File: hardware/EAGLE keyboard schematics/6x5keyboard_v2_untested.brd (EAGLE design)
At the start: 117.8 x 116.8 mm, 71 parts

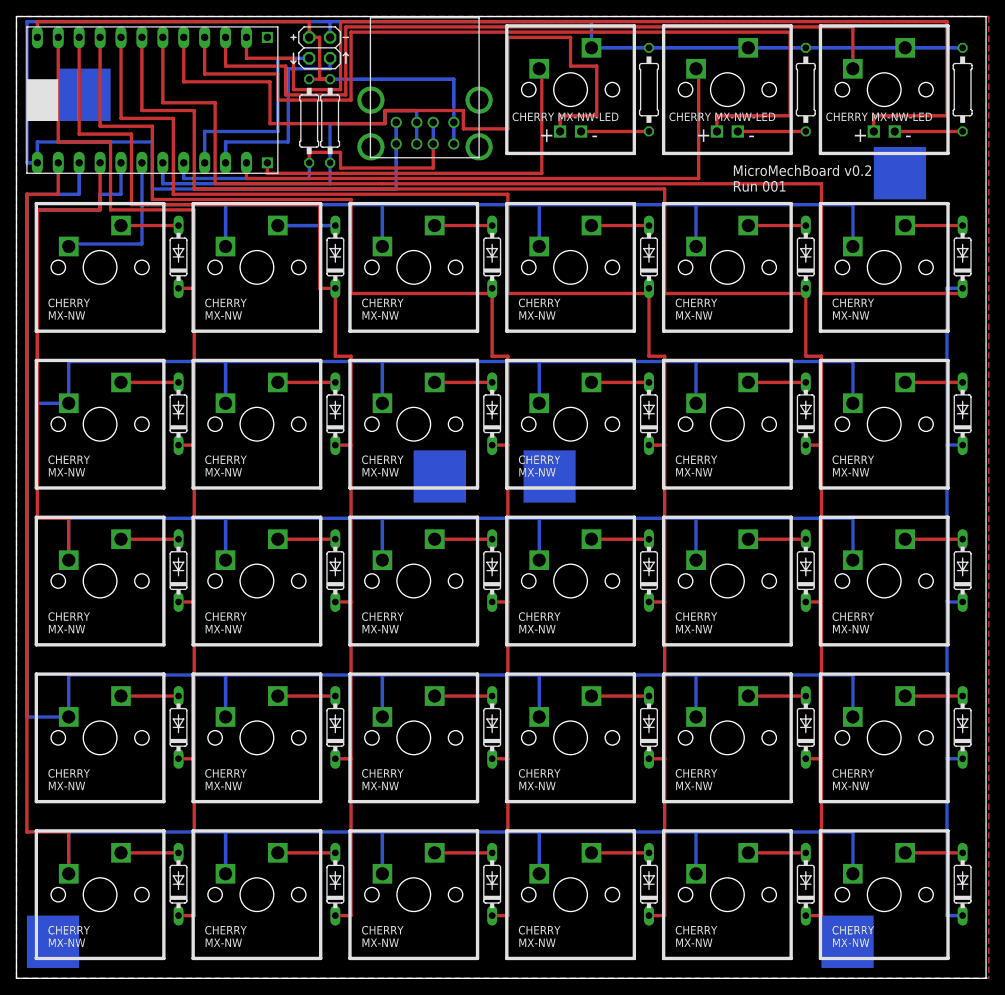
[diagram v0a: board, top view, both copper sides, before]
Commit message: Board routed with groovy looking traces, using freerouting.net
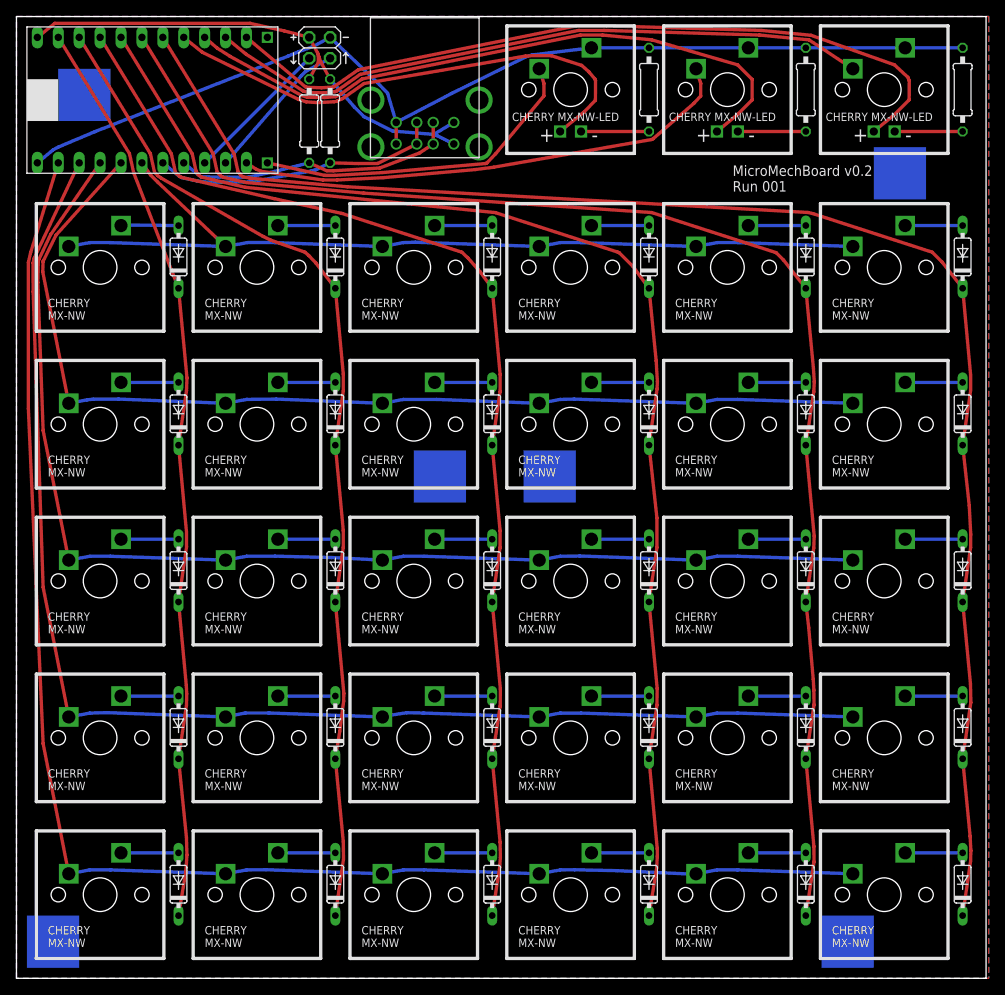
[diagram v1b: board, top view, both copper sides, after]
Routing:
- net GND: track 197.1 -> 125.7 mm
- net N$39: track 168.9 -> 128.4 mm
- net N$37: track 204.5 -> 164.4 mm
- net N$38: track 185.4 -> 146.3 mm
- net N$41: track 221.0 -> 182.8 mm
- net N$47: track 91.8 -> 62.1 mm
- net N$46: track 108.0 -> 79.2 mm
- net N$54: track 121.9 -> 93.5 mm
- net N$36: track 214.6 -> 186.7 mm
- net N$35: track 198.1 -> 170.3 mm
- net N$34: track 181.6 -> 153.9 mm
- net N$33: track 165.1 -> 137.5 mm
- net N$32: track 147.3 -> 122.1 mm
- net N$31: track 132.7 -> 110.7 mm
- net N$40: track 130.8 -> 109.9 mm
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
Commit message: Changed all rectangles into proper SMD pads.
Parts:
- added U$36, U$37, U$38, U$39, U$40, U$41: MOUNTING-PAD, my_parts:MOUNTING-PAD
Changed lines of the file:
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@@
 <wire x1="119.05" y1="130.8" x2="1.27" y2="130.8" width="0" layer="20"/>
 <wire x1="1.27" y1="130.8" x2="1.27" y2="13.97" width="0" layer="20"/>
-<rectangle x1="6.35" y1="118.11" x2="12.7" y2="124.46" layer="16"/>
-<rectangle x1="6.35" y1="118.11" x2="12.7" y2="124.46" layer="30"/>
-<rectangle x1="105.41" y1="108.585" x2="111.76" y2="114.935" layer="16"/>
-<rectangle x1="105.41" y1="108.585" x2="111.76" y2="114.935" layer="30"/>
-<rectangle x1="2.54" y1="15.24" x2="8.89" y2="21.59" layer="16"/>
-<rectangle x1="2.54" y1="15.24" x2="8.89" y2="21.59" layer="30"/>
-<rectangle x1="99.06" y1="15.24" x2="105.41" y2="21.59" layer="16"/>
-<rectangle x1="99.06" y1="15.24" x2="105.41" y2="21.59" layer="30"/>
-<rectangle x1="49.53" y1="71.755" x2="55.88" y2="78.105" layer="16"/>
-<rectangle x1="49.53" y1="71.755" x2="55.88" y2="78.105" layer="30"/>
-<rectangle x1="62.865" y1="71.755" x2="69.215" y2="78.105" layer="16"/>
-<rectangle x1="62.865" y1="71.755" x2="69.215" y2="78.105" layer="30"/>
 <wire x1="34.925" y1="126.365" x2="34.925" y2="125.095" width="0.1778" layer="21"/>
 <wire x1="34.925" y1="125.095" x2="35.2425" y2="125.4125" width="0.1778" layer="21"/>
@@
 <element name="JP1" library="pinhead" package="2X02" value="UART" x="38.1" y="127" smashed="yes" rot="R270"/>
 <element name="U$35" library="my_parts" package="DUAL-USB-A" value="DUAL-USB-A" x="57.4675" y="120.65" rot="R180"/>
+<element name="U$36" library="my_parts" package="MOUNTING-PAD" value="MOUNTING-PAD" x="5.715" y="18.415"/>
+<element name="U$37" library="my_parts" package="MOUNTING-PAD" value="MOUNTING-PAD" x="102.235" y="18.415"/>
+<element name="U$38" library="my_parts" package="MOUNTING-PAD" value="MOUNTING-PAD" x="52.705" y="74.93"/>
+<element name="U$39" library="my_parts" package="MOUNTING-PAD" value="MOUNTING-PAD" x="66.04" y="74.93"/>
+<element name="U$40" library="my_parts" package="MOUNTING-PAD" value="MOUNTING-PAD" x="9.525" y="121.285"/>
+<element name="U$41" library="my_parts" package="MOUNTING-PAD" value="MOUNTING-PAD" x="108.585" y="111.76"/>
 </elements>
 <signals>
